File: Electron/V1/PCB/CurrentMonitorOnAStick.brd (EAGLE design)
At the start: 89.5 x 29.3 mm, 21 parts, among them IC1 7805DT, U1 INA219AIDCNRSOIC

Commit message: Moved pcb files to PCB subfolder.
Added datasheets
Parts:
- D1, D2: value (none) -> MBRA140T3G
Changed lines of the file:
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@@
 <vertex x="52.705" y="22.86"/>
 <vertex x="52.705" y="20.32"/>
-<vertex x="61.595" y="20.32"/>
 </polygon>
 <polygon width="0.4064" layer="41">
@@
 </element>
 <element name="IC1" library="linear" package="TO252" value="7805DT" x="43.18" y="12.7" smashed="yes" rot="R270"/>
-<element name="D1" library="SparkFun-DiscreteSemi" package="SMA-DIODE" value="" x="34.29" y="7.3025" smashed="yes" rot="R180">
+<element name="D1" library="SparkFun-DiscreteSemi" package="SMA-DIODE" value="MBRA140T3G" x="34.29" y="7.3025" smashed="yes" rot="R180">
 <attribute name="NAME" x="33.909" y="8.9535" size="0.8128" layer="25"/>
 <attribute name="VALUE" x="34.036" y="5.6515" size="0.4064" layer="27" rot="R180"/>
 </element>
-<element name="D2" library="SparkFun-DiscreteSemi" package="SMA-DIODE" value="" x="23.8125" y="9.525" smashed="yes" rot="R270">
+<element name="D2" library="SparkFun-DiscreteSemi" package="SMA-DIODE" value="MBRA140T3G" x="23.8125" y="9.525" smashed="yes" rot="R270">
 <attribute name="NAME" x="23.114" y="13.081" size="0.8128" layer="25"/>
 <attribute name="VALUE" x="25.4635" y="9.271" size="0.4064" layer="27" rot="R270"/>

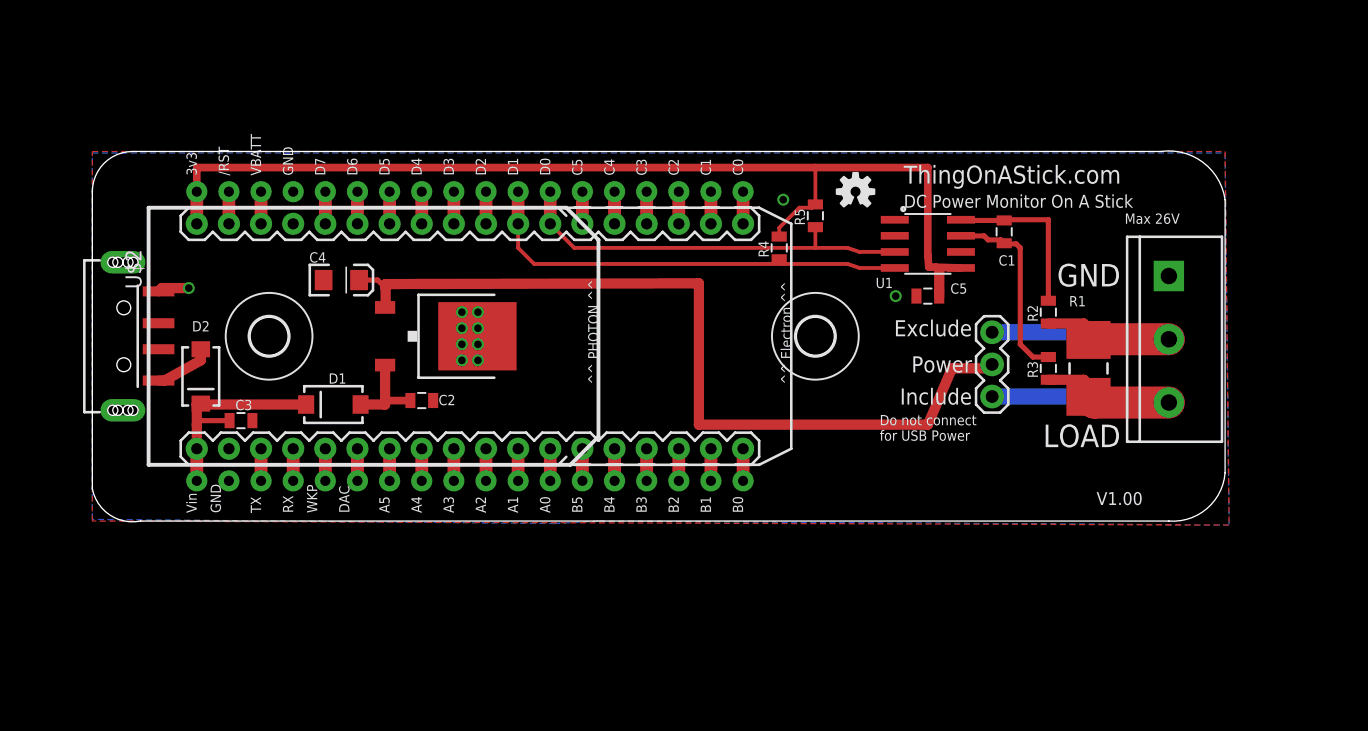
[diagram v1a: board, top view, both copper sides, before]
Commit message: Bumped to V1.1
Added second connector to allow input and output connectors to be different whilst still allowing the single connector.

Moved the mounting holes around a little.

Metricified it so dimensions and mounting holes work nicely in mm.

Added reverse mount OSH LED.
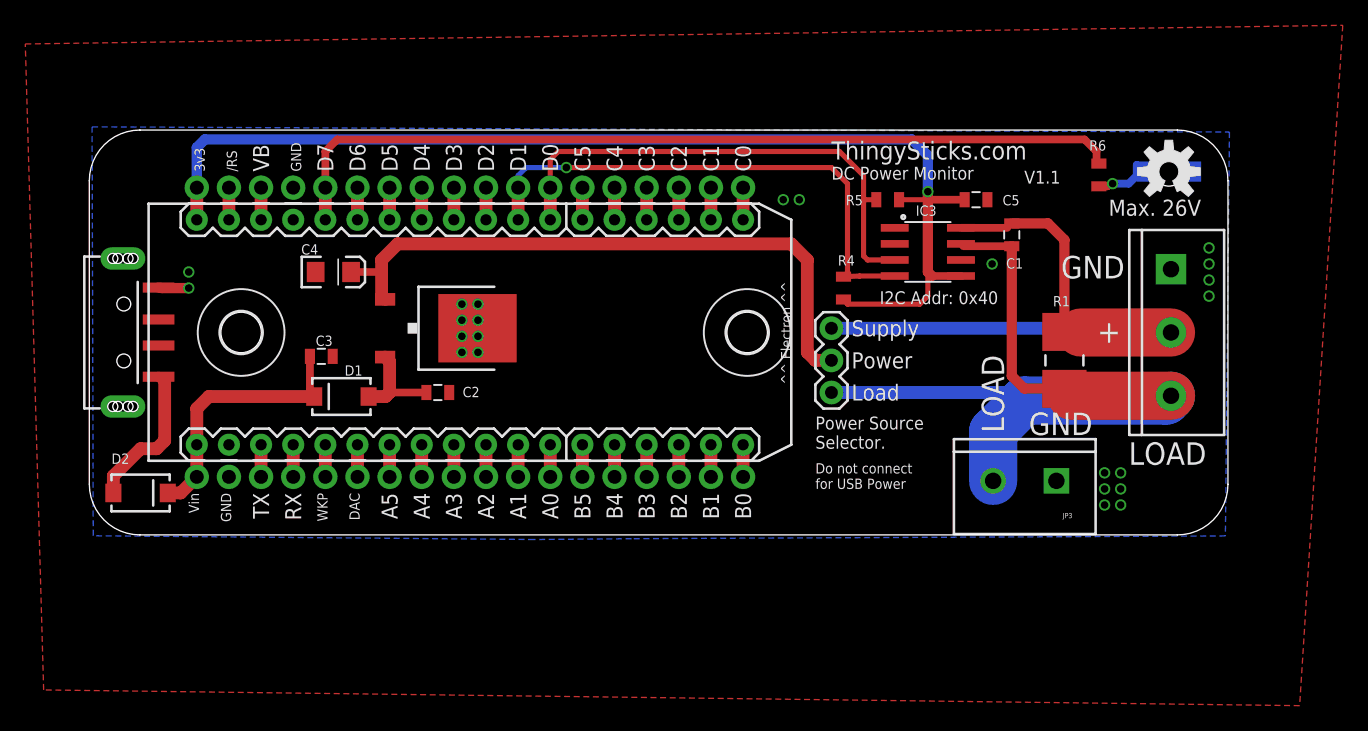
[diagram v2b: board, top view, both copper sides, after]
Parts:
- removed LOGO2: OSHW-LOGOS, SparkFun-Aesthetics:OSHW-LOGO-S
- removed R2, R3: 0R, SparkFun-Resistors:0805
- removed U$2: ELECTRONDUALNAMED, Tinamous:ELECTRON_SIMPLE_SILK_NAMES_DUAL
- removed U1: INA219AIDCNRSOIC, INA219AIDCNR:SO08
- added D3: (no value), SparkFun-LED:LED-1206-BOTTOM
- added FRAME2: FRAME-LETTER, SparkFun-Aesthetics:CREATIVE_COMMONS
- added IC2: ELECTRONDUALNAMED, Tinamous:ELECTRON_SIMPLE_SILK_NAMES_DUAL
- added IC3: INA219AIDCNRSOIC, INA219AIDCNR:SO08
- added JP3: (no value), SparkFun-Connectors:SCREWTERMINAL-5MM-2
- added LOGO1: OSHW-LOGOM, SparkFun-Aesthetics:OSHW-LOGO-M
- added R6: 1k5, SparkFun-Resistors:0805
- H1, H2: value MOUNT-HOLE3.0 -> MOUNT-HOLE3.2; device holes:3,0 -> holes:3,2
- R4, R5: value 4k7 -> (none)
- moved JP2 12.7 mm to (73.7, 13.3)
- moved D2 10.4 mm to (19.1, 0.32), turned to 0 degrees
- moved C5 8.52 mm to (85.1, 23.5), turned to 180 degrees
- moved C3 8.13 mm to (33.3, 11.1)
- moved R4 5.99 mm to (74.6, 16.5), turned to 270 degrees
- moved R5 5.85 mm to (78.1, 23.5), turned to 0 degrees
- moved H2 5.40 mm to (67.0, 13.0)
- moved H1 2.23 mm to (27.0, 13.0)
- moved R1 2.01 mm to (92.1, 10.8)
- moved C2 1.42 mm to (42.5, 8.26)
- moved C4 0.90 mm to (34.3, 17.8)
- moved D1 0.90 mm to (34.9, 7.94)
- moved C1 0.64 mm to (87.9, 20.7)
- moved IC1 0.64 mm to (43.2, 13.3)
- moved JP1 0.56 mm to (100.5, 18.0)
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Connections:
- removed net N$11: U$2.D7, U$2.D7_1
- removed net N$12: C1.2, R3.2, U1.7
- removed net N$4: C1.1, R2.2, U1.8
- new net D7: IC2.D7, IC2.D7_1, R6.2
- new net N$13: D3.A, R6.1
- net 3.3V: now also IC2.3V3, IC2.3V3_1, IC3.5; no longer U$2.3V3, U$2.3V3_1, U1.5
- net 5V: now also IC2.VIN, IC2.VIN_1B; no longer U$2.VIN, U$2.VIN_1B
- net GND: now also D3.C, IC2.GND, IC2.GND@2, IC2.GND_1, IC2.GND_1B, IC3.1, IC3.2, IC3.6, JP3.1; no longer U$2.GND, U$2.GND@2, U$2.GND_1, U$2.GND_1B, U1.1, U1.2, U1.6
- net LOAD+: now also C1.2, IC3.7, JP3.2; no longer R3.1
- net N$15: now also IC2.D6, IC2.D6_1; no longer U$2.D6, U$2.D6_1
- net N$16: now also IC2.D5, IC2.D5_1; no longer U$2.D5, U$2.D5_1
- net N$20: now also IC2.D4, IC2.D4_1; no longer U$2.D4, U$2.D4_1
- net N$21: now also IC2.D3, IC2.D3_1; no longer U$2.D3, U$2.D3_1
- net N$22: now also IC2.D2, IC2.D2_1; no longer U$2.D2, U$2.D2_1
- net N$23: now also IC2.C5, IC2.C5_1; no longer U$2.C5, U$2.C5_1
- net N$24: now also IC2.C4, IC2.C4_1; no longer U$2.C4, U$2.C4_1
- net N$25: now also IC2.C3, IC2.C3_1; no longer U$2.C3, U$2.C3_1
- net N$26: now also IC2.C2, IC2.C2_1; no longer U$2.C2, U$2.C2_1
- net N$28: now also IC2.C1, IC2.C1_1; no longer U$2.C1, U$2.C1_1
- net N$29: now also IC2.C0, IC2.C0_1; no longer U$2.C0, U$2.C0_1
- net N$31: now also IC2.B0, IC2.B0_1; no longer U$2.B0, U$2.B0_1
- net N$33: now also IC2.B1, IC2.B1_1; no longer U$2.B1, U$2.B1_1
- net N$35: now also IC2.B2, IC2.B2_1; no longer U$2.B2, U$2.B2_1
- net N$36: now also IC2.B3, IC2.B3_1; no longer U$2.B3, U$2.B3_1
- net N$37: now also IC2.B4, IC2.B4_1; no longer U$2.B4, U$2.B4_1
- net N$38: now also IC2.B5, IC2.B5_1; no longer U$2.B5, U$2.B5_1
- net N$39: now also IC2.A0, IC2.A0_1; no longer U$2.A0, U$2.A0_1
- net N$40: now also IC2.A1, IC2.A1_1; no longer U$2.A1, U$2.A1_1
- net N$41: now also IC2.A2, IC2.A2_1; no longer U$2.A2, U$2.A2_1
- net N$42: now also IC2.A3, IC2.A3_1; no longer U$2.A3, U$2.A3_1
- net N$43: now also IC2.A4, IC2.A4_1; no longer U$2.A4, U$2.A4_1
- net N$44: now also IC2.A5, IC2.A5_1; no longer U$2.A5, U$2.A5_1
- net N$45: now also IC2.DAC, IC2.DAC_1; no longer U$2.DAC, U$2.DAC_1
- net N$46: now also IC2.WKP, IC2.WKP_1; no longer U$2.WKP, U$2.WKP_1
- net N$47: now also IC2.RX, IC2.RX_1; no longer U$2.RX, U$2.RX_1
- net N$48: now also IC2.TX, IC2.TX_1; no longer U$2.TX, U$2.TX_1
- net N$6: now also IC2.VBAT, IC2.VBATT_1; no longer U$2.VBAT, U$2.VBATT_1
- net N$7: now also IC2.RST, IC2.RST_1; no longer U$2.RST, U$2.RST_1
- net SCL: now also IC2.D1, IC2.D1_1, IC3.4; no longer U$2.D1, U$2.D1_1, U1.4
- net SDA: now also IC2.D0, IC2.D0_1, IC3.3; no longer U$2.D0, U$2.D0_1, U1.3
- net SUPPLY+: now also C1.1, IC3.8; no longer R2.1
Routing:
- net D7: track 0.00 -> 68.2 mm
- net LOAD+: track 25.0 -> 65.1 mm
- net SUPPLY+: track 23.9 -> 52.0 mm
- net VIN: track 66.4 -> 49.8 mm
- net N$12: track 15.3 -> 0.00 mm
- net N$4: track 13.4 -> 0.00 mm
- net 3.3V: track 84.8 -> 93.3 mm, vias 0 -> 1
- net SDA: track 32.2 -> 40.5 mm
- net N$1: track 4.63 -> 11.9 mm
- net SCL: track 35.3 -> 41.9 mm, vias 0 -> 1
- net N$13: track 0.00 -> 5.06 mm, vias 0 -> 1
- net 5V: track 18.3 -> 21.7 mm
- net N$11: track 2.54 -> 0.00 mm
- net N$3: track 7.05 -> 7.65 mm
- net GND: track 2.49 -> 2.39 mm, vias 11 -> 23
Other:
- board size 89.5 x 29.3 mm -> 90 x 32 mm
- board text added: "+"
- board text added: "9 August 2017"
- board text added: "DC Power Monitor"
- board text added: "I2C Addr: 0x40"
- board text added: "Load"
- board text added: "Max. 26V"
- board text added: "Power Source Selector."
- board text added: "S.Harrison"
- board text added: "Supply"
- board text added: "ThingySticks.com"
- board text added: "ThingySticks.com/CurrentMonitor"
- board text added: "V1.1"
- board text added: "github.com/ThingySticks/CurrentMonitor"
- board text removed: "DC Power Monitor On A Stick"
- board text removed: "Exclude"
- board text removed: "Include"
- board text removed: "Max 26V"
- board text removed: "ThingOnAStick.com"
- board text removed: "V1.00"
- board text removed: "^^ PHOTON ^^"
